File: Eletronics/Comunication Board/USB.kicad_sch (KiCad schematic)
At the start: 6 parts, among them J1 USB_C_Receptacle_USB2.0

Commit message: alteracoes finais
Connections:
- net USB_D+: now also J1.A6 (D+), J1.B6 (D+); no longer J1.A7 (D-), J1.B7 (D-)
- net USB_D-: now also J1.A7 (D-), J1.B7 (D-); no longer J1.A6 (D+), J1.B6 (D+)

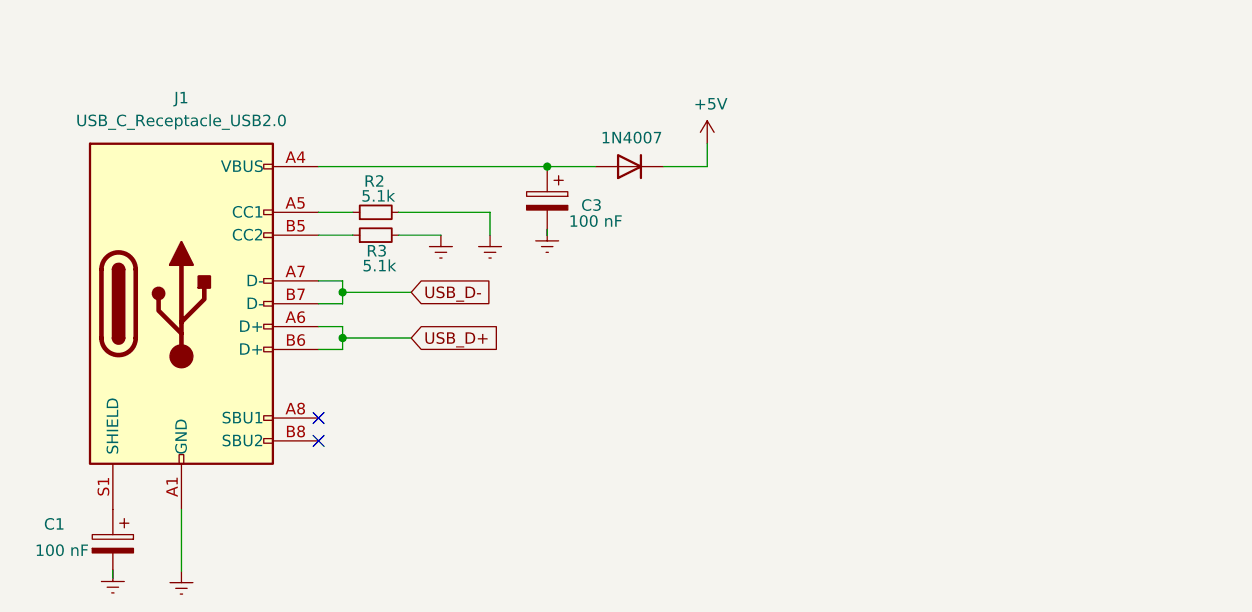
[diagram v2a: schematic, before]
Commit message: Revisão com alterações apontadas no esquemático
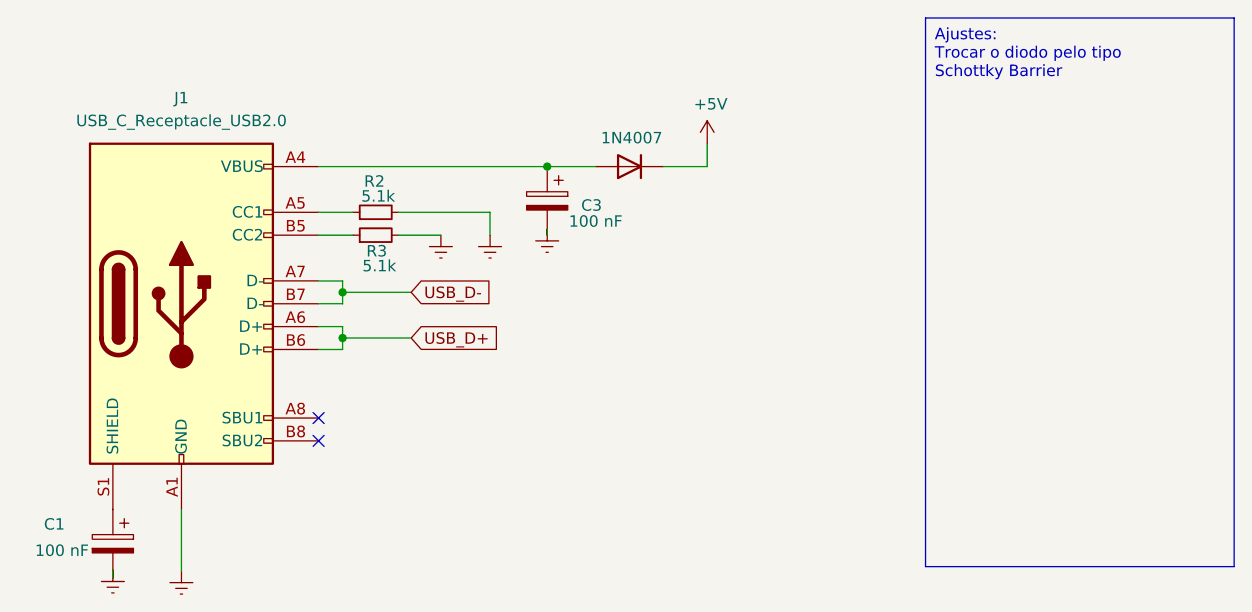
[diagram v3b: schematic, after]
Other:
- company: (none) -> Project Neon
- title: (none) -> Placa de comunicação
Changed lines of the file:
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@@
 	(generator_version "8.0")
 	(paper "A4")
+	(title_block
+		(title "Placa de comunicação")
+		(date "2024-05-04")
+		(rev "0")
+		(company "Project Neon")
+		(comment 1 "Autor: Leticia Martins")
+		(comment 2 "Revisão: Marcus Holanda")
+		(comment 3 "Documento com alterações necessárias, não é um docuemnto final")
+	)
 	(junction
 		(at 143.51 87.63)
@@
 		)
 	)
+	(text_box "Ajustes:\nTrocar o diodo pelo tipo Schottky Barrier"
+		(exclude_from_sim no)
+		(at 208.28 52.07 0)
+		(size 34.29 60.96)
+		(stroke
+			(width 0)
+			(type default)
+		)
+		(fill
+			(type none)
+		)
+		(effects
+			(font
+				(size 1.27 1.27)
+			)
+			(justify left top)
+		)
+	)
